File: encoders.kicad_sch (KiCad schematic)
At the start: 110 parts, among them U1 PEL12T-4225S-S1024, U10 WS2811F, U11 WS2811F, U12 WS2811F, U13 WS2811F, U14 WS2811F, U15 WS2811F, U16 WS2811F, U2 PEL12T-4225S-S1024, U3 PEL12T-4225S-S1024, U30 MCP23S17_SS, U31 MCP23S17_SS, U4 PEL12T-4225S-S1024, U5 PEL12T-4225S-S1024, U6 PEL12T-4225S-S1024, U7 PEL12T-4225S-S1024, U8 PEL12T-4225S-S1024, U9 WS2811F

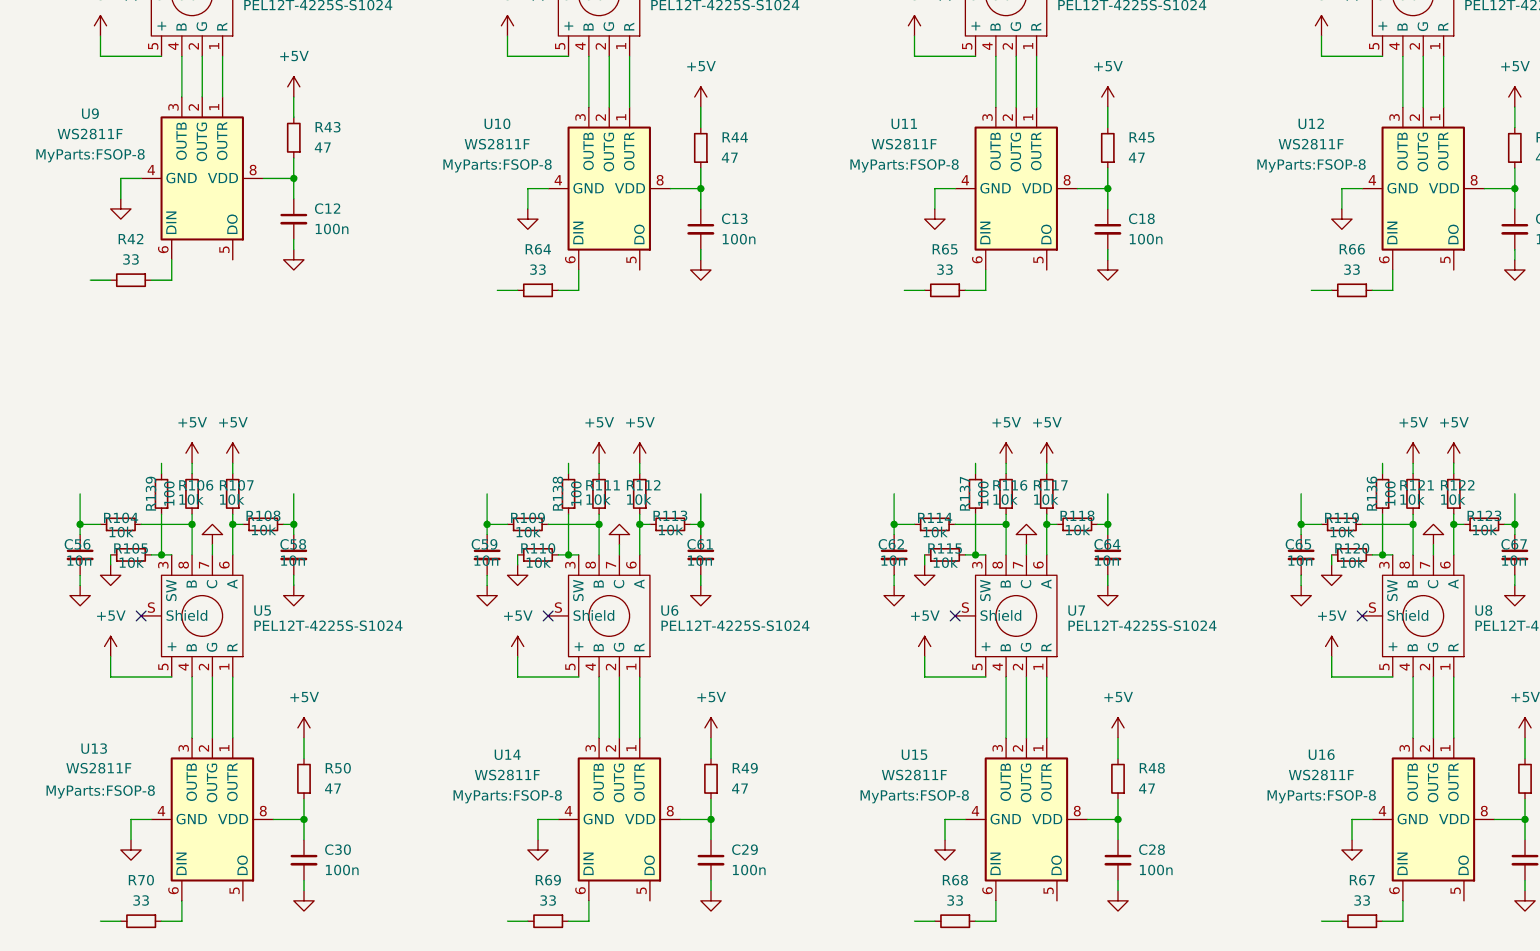
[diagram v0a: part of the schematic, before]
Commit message: rename symbol & footprint libs
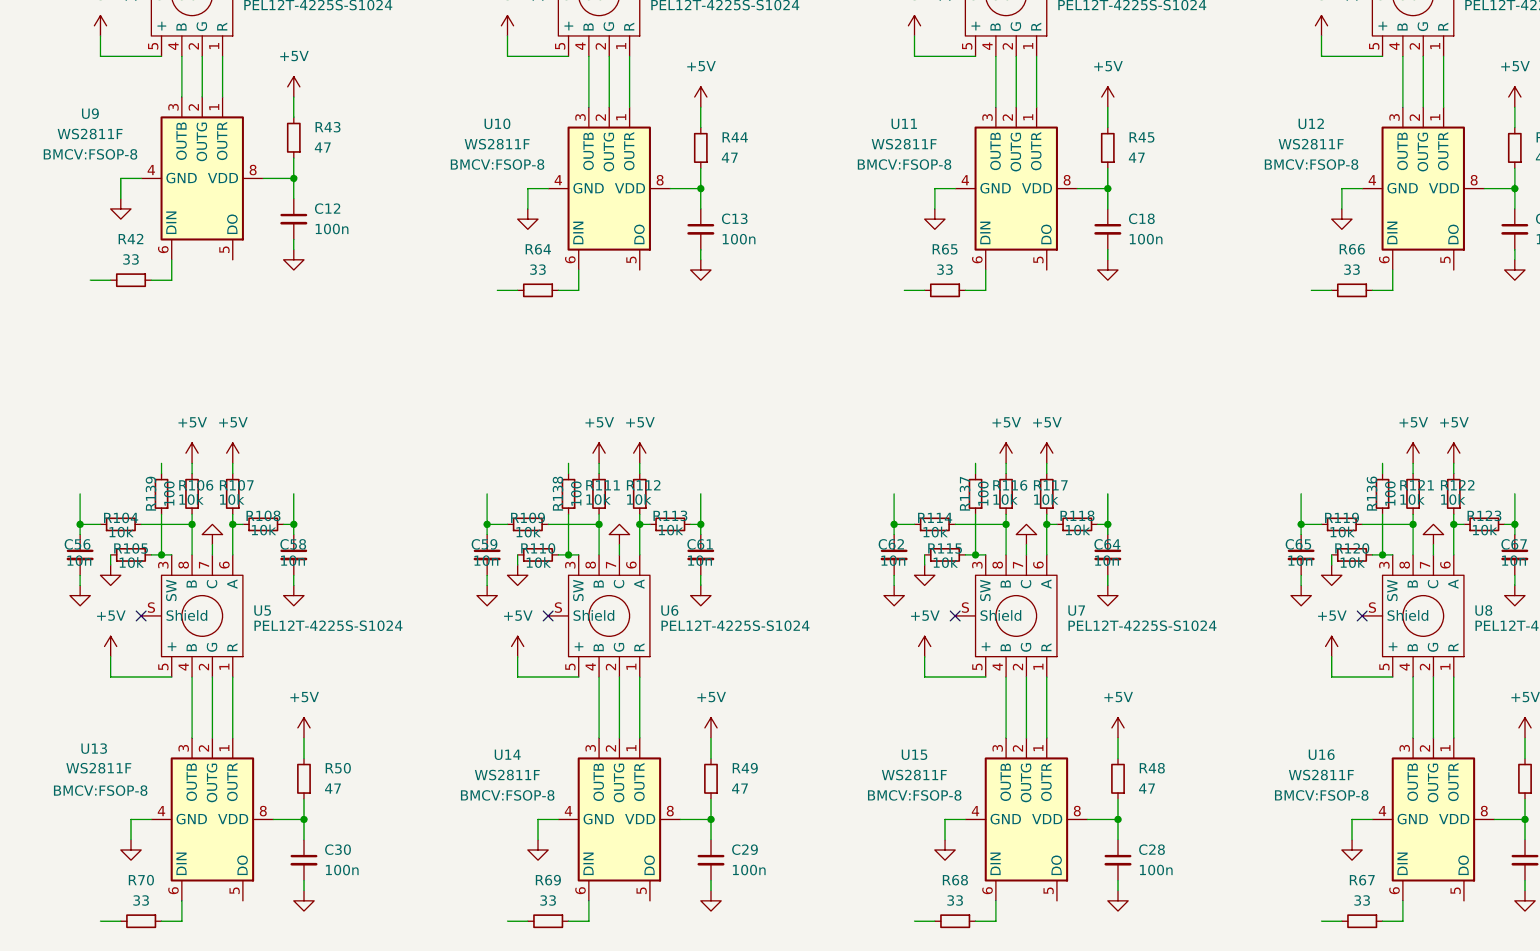
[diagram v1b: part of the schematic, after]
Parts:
- U1, U2, U3, U4, U5, U6, U7, U8: footprint MyParts:PEL12T-4xxxS-S1024 -> BMCV:PEL12T-4xxxS-S1024; symbol MySymbols:EC12PLRGBSDVBF -> BMCV:EC12PLRGBSDVBF
- U10, U11, U12, U13, U14, U15, U16, U9: footprint MyParts:FSOP-8 -> BMCV:FSOP-8; symbol MySymbols:WS2811 -> BMCV:WS2811
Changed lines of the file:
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@@
 	)
 	(symbol
-		(lib_id "MySymbols:EC12PLRGBSDVBF")
+		(lib_id "BMCV:EC12PLRGBSDVBF")
 		(at 39.37 115.57 180)
 		(unit 1)
@@
 			)
 		)
-		(property "Footprint" "MyParts:PEL12T-4xxxS-S1024"
+		(property "Footprint" "BMCV:PEL12T-4xxxS-S1024"
 			(at 39.37 115.57 0)
 			(effects
@@
 	)
 	(symbol
-		(lib_id "MySymbols:EC12PLRGBSDVBF")
+		(lib_id "BMCV:EC12PLRGBSDVBF")
 		(at 191.77 115.57 180)
 		(unit 1)
@@
 			)
 		)
-		(property "Footprint" "MyParts:PEL12T-4xxxS-S1024"
+		(property "Footprint" "BMCV:PEL12T-4xxxS-S1024"
 			(at 191.77 115.57 0)
 			(effects
@@
 	)
 	(symbol
-		(lib_id "MySymbols:EC12PLRGBSDVBF")
+		(lib_id "BMCV:EC12PLRGBSDVBF")
 		(at 190.5 38.1 180)
 		(unit 1)
@@
 			)
 		)
-		(property "Footprint" "MyParts:PEL12T-4xxxS-S1024"
+		(property "Footprint" "BMCV:PEL12T-4xxxS-S1024"
 			(at 190.5 38.1 0)
 			(effects
@@
 	)
 	(symbol
-		(lib_id "MySymbols:EC12PLRGBSDVBF")
+		(lib_id "BMCV:EC12PLRGBSDVBF")
 		(at 140.97 115.57 180)
 		(unit 1)
@@
 			)
 		)
-		(property "Footprint" "MyParts:PEL12T-4xxxS-S1024"
+		(property "Footprint" "BMCV:PEL12T-4xxxS-S1024"
 			(at 140.97 115.57 0)
 			(effects
@@
 	)
 	(symbol
-		(lib_id "MySymbols:WS2811")
+		(lib_id "BMCV:WS2811")
 		(at 140.97 62.23 270)
 		(mirror x)
@@
 			)
 		)
-		(property "Footprint" "MyParts:FSOP-8"
+		(property "Footprint" "BMCV:FSOP-8"
 			(at 127 59.2738 90)
 			(effects
@@
 	)
 	(symbol
-		(lib_id "MySymbols:EC12PLRGBSDVBF")
+		(lib_id "BMCV:EC12PLRGBSDVBF")
 		(at 90.17 115.57 180)
 		(unit 1)
@@
 			)
 		)
-		(property "Footprint" "MyParts:PEL12T-4xxxS-S1024"
+		(property "Footprint" "BMCV:PEL12T-4xxxS-S1024"
 			(at 90.17 115.57 0)
 			(effects
@@
 	)
 	(symbol
-		(lib_id "MySymbols:WS2811")
+		(lib_id "BMCV:WS2811")
 		(at 90.17 62.23 270)
 		(mirror x)
@@
 			)
 		)
-		(property "Footprint" "MyParts:FSOP-8"
+		(property "Footprint" "BMCV:FSOP-8"
 			(at 76.2 59.2738 90)
 			(effects
@@
 	)
 	(symbol
-		(lib_id "MySymbols:WS2811")
+		(lib_id "BMCV:WS2811")
 		(at 193.04 140.97 270)
 		(mirror x)
@@
 			)
 		)
-		(property "Footprint" "MyParts:FSOP-8"
+		(property "Footprint" "BMCV:FSOP-8"
 			(at 179.07 138.0138 90)
 			(effects
@@
 	)
 	(symbol
-		(lib_id "MySymbols:EC12PLRGBSDVBF")
+		(lib_id "BMCV:EC12PLRGBSDVBF")
 		(at 88.9 38.1 180)
 		(unit 1)
@@
 			)
 		)
-		(property "Footprint" "MyParts:PEL12T-4xxxS-S1024"
+		(property "Footprint" "BMCV:PEL12T-4xxxS-S1024"
 			(at 88.9 38.1 0)
 			(effects
@@
 	)
 	(symbol
-		(lib_id "MySymbols:WS2811")
+		(lib_id "BMCV:WS2811")
 		(at 142.24 140.97 270)
 		(mirror x)
@@
 			)
 		)
-		(property "Footprint" "MyParts:FSOP-8"
+		(property "Footprint" "BMCV:FSOP-8"
 			(at 128.27 138.0138 90)
 			(effects
@@
 	)
 	(symbol
-		(lib_id "MySymbols:WS2811")
+		(lib_id "BMCV:WS2811")
 		(at 91.44 140.97 270)
 		(mirror x)
@@
 			)
 		)
-		(property "Footprint" "MyParts:FSOP-8"
+		(property "Footprint" "BMCV:FSOP-8"
 			(at 77.47 138.0138 90)
 			(effects
@@
 	)
 	(symbol
-		(lib_id "MySymbols:WS2811")
+		(lib_id "BMCV:WS2811")
 		(at 39.37 60.96 270)
 		(mirror x)
@@
 			)
 		)
-		(property "Footprint" "MyParts:FSOP-8"
+		(property "Footprint" "BMCV:FSOP-8"
 			(at 25.4 58.0038 90)
 			(effects
@@
 	)
 	(symbol
-		(lib_id "MySymbols:EC12PLRGBSDVBF")
+		(lib_id "BMCV:EC12PLRGBSDVBF")
 		(at 139.7 38.1 180)
 		(unit 1)
@@
 			)
 		)
-		(property "Footprint" "MyParts:PEL12T-4xxxS-S1024"
+		(property "Footprint" "BMCV:PEL12T-4xxxS-S1024"
 			(at 139.7 38.1 0)
 			(effects
@@
 	)
 	(symbol
-		(lib_id "MySymbols:WS2811")
+		(lib_id "BMCV:WS2811")
 		(at 191.77 62.23 270)
 		(mirror x)
@@
 			)
 		)
-		(property "Footprint" "MyParts:FSOP-8"
+		(property "Footprint" "BMCV:FSOP-8"
 			(at 177.8 59.2738 90)
 			(effects
@@
 	)
 	(symbol
-		(lib_id "MySymbols:WS2811")
+		(lib_id "BMCV:WS2811")
 		(at 40.64 140.97 270)
 		(mirror x)
@@
 			)
 		)
-		(property "Footprint" "MyParts:FSOP-8"
+		(property "Footprint" "BMCV:FSOP-8"
 			(at 26.67 137.414 90)
 			(effects
@@
 	)
 	(symbol
-		(lib_id "MySymbols:EC12PLRGBSDVBF")
+		(lib_id "BMCV:EC12PLRGBSDVBF")
 		(at 38.1 38.1 180)
 		(unit 1)
@@
 			)
 		)
-		(property "Footprint" "MyParts:PEL12T-4xxxS-S1024"
+		(property "Footprint" "BMCV:PEL12T-4xxxS-S1024"
 			(at 38.1 38.1 0)
 			(effects

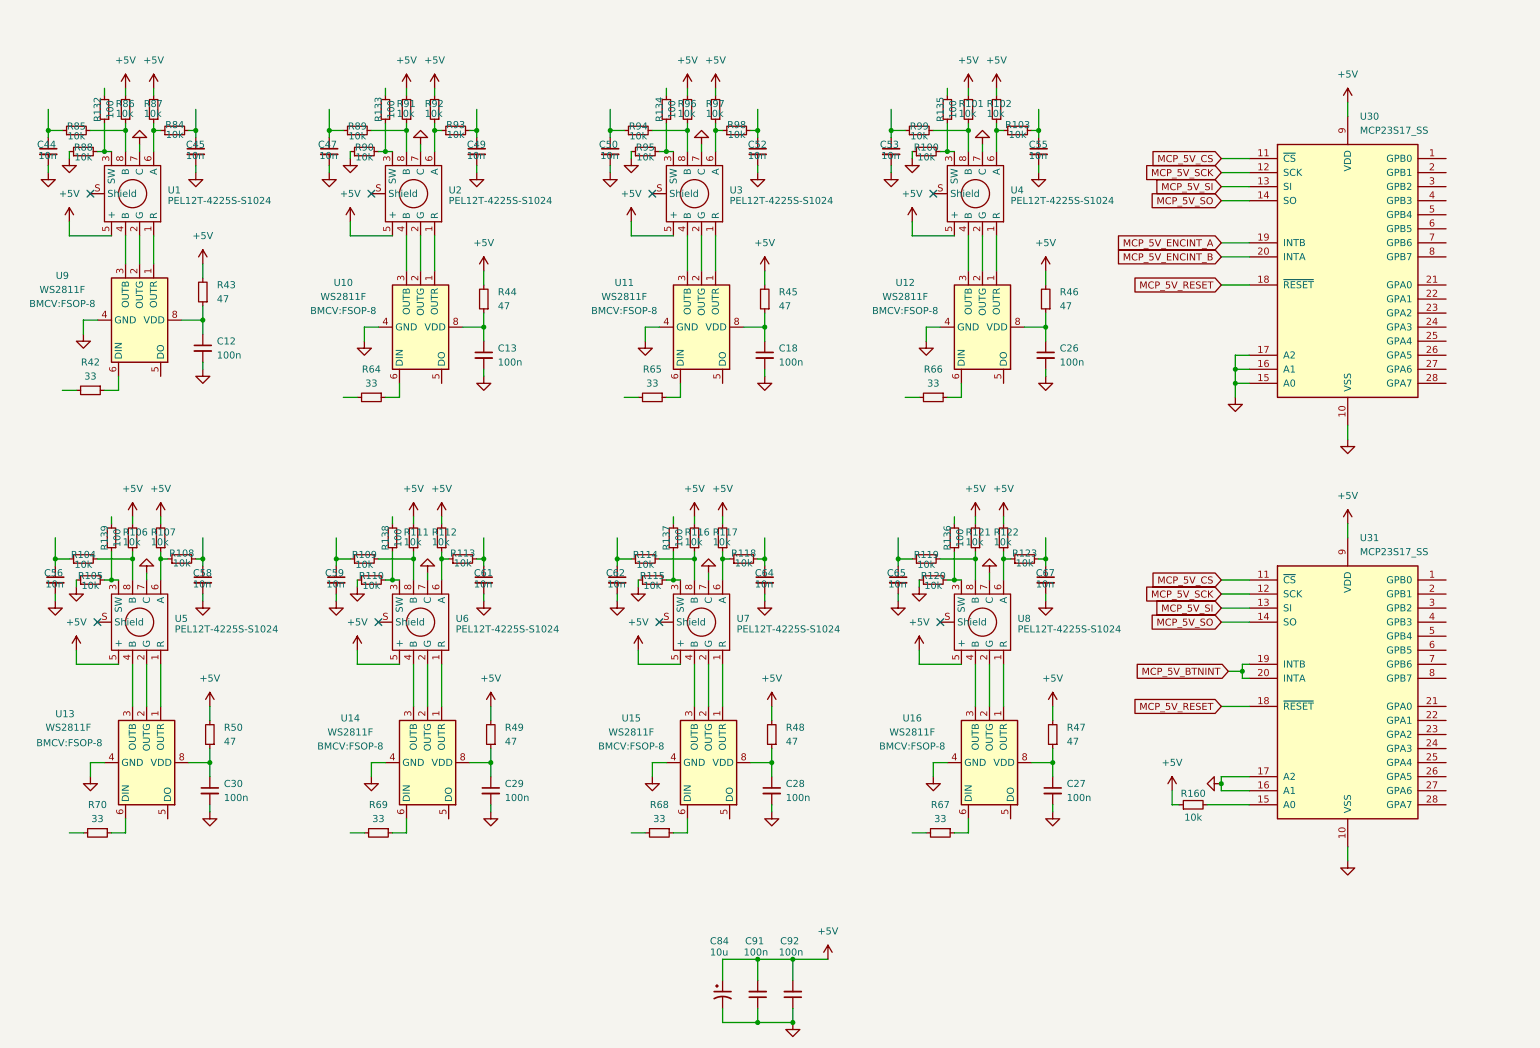
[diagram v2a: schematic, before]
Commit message: routing progress (bottom buttons & encoders)
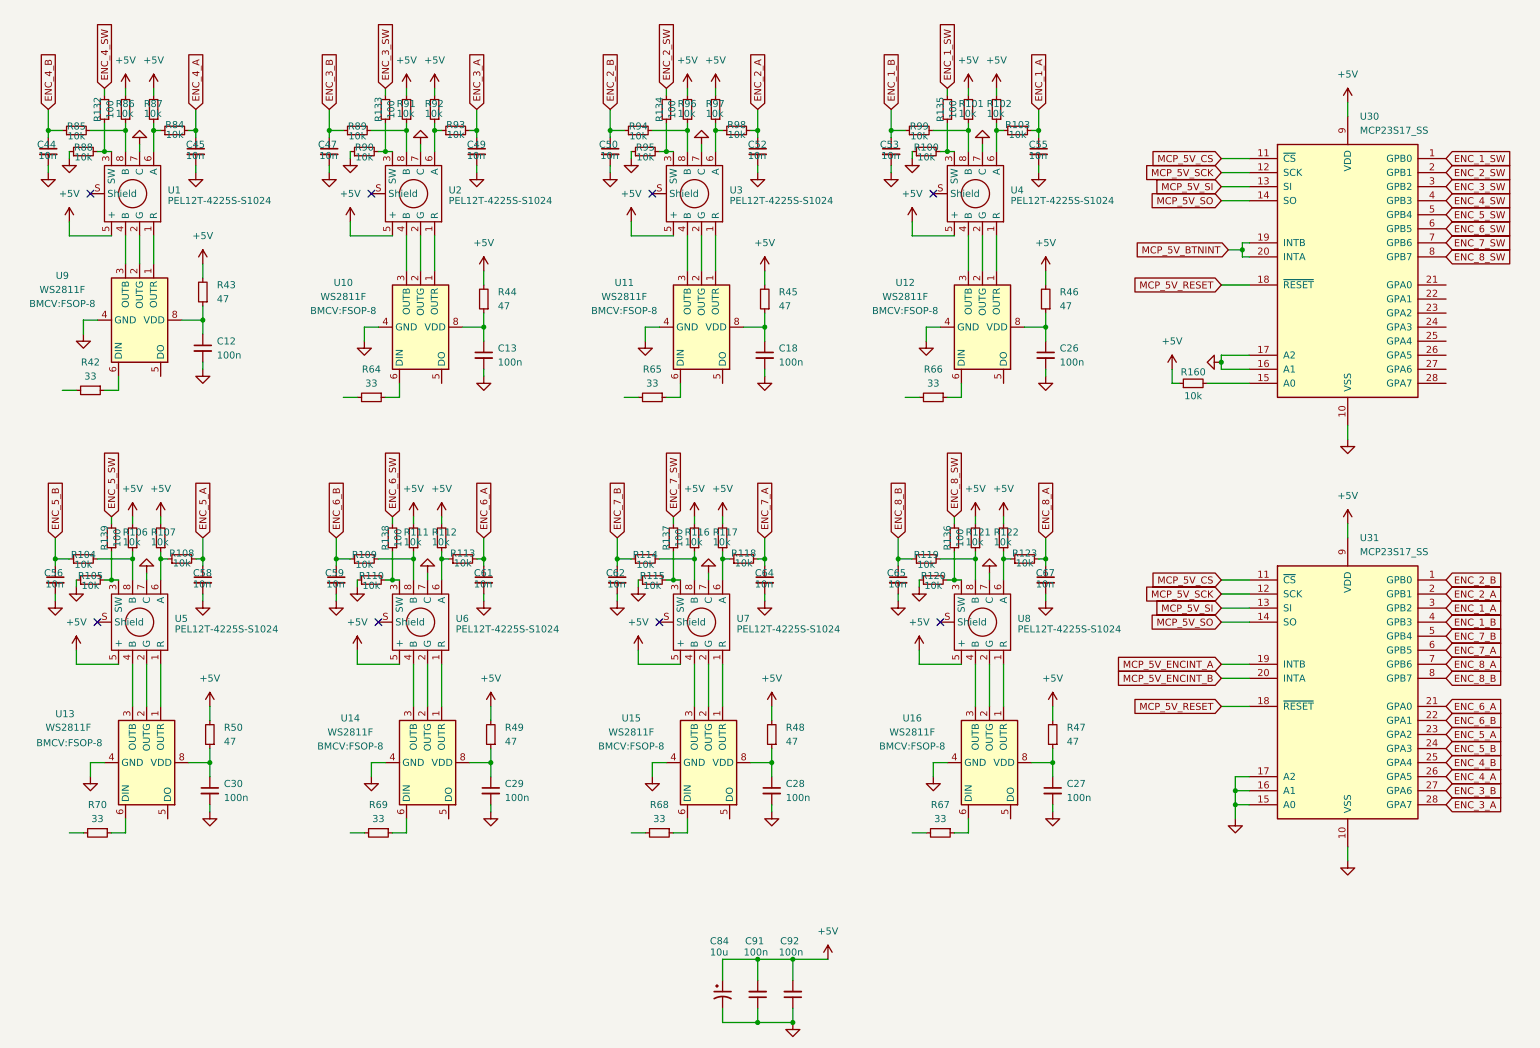
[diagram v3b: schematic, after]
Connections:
- net GND: now also U31.15 (A0); no longer U30.15 (A0)
- net MCP_5V_BTNINT: now also U30.19 (INTB), U30.20 (INTA); no longer U31.19 (INTB), U31.20 (INTA)
- net MCP_5V_ENCINT_A: now also U31.19 (INTB); no longer U30.19 (INTB)
- net MCP_5V_ENCINT_B: now also U31.20 (INTA); no longer U30.20 (INTA)
- net ENC_3_B: now reaches C47.1, R89.1
- net ENC_3_B: now also U31.27 (GPA6)
- net ENC_5_A: now reaches C58.1, R108.2
- net ENC_5_A: now also U31.23 (GPA2)
- net ENC_7_A: now reaches C64.1, R118.2
- net ENC_7_A: now also U31.6 (GPB5)
- net ENC_1_A: now reaches C55.1, R103.2
- net ENC_1_A: now also U31.3 (GPB2)
- net ENC_5_B: now reaches C56.1, R104.1
- net ENC_5_B: now also U31.24 (GPA3)
- net ENC_8_B: now reaches C65.1, R119.1
- net ENC_8_B: now also U31.8 (GPB7)
- net ENC_2_A: now reaches C52.1, R98.2
- net ENC_2_A: now also U31.2 (GPB1)
- net ENC_4_A: now reaches C45.1, R84.2
- net ENC_4_A: now also U31.26 (GPA5)
- net ENC_8_A: now reaches C67.1, R123.2
- net ENC_8_A: now also U31.7 (GPB6)
- net ENC_4_B: now reaches C44.1, R85.1
- net ENC_4_B: now also U31.25 (GPA4)
- net ENC_2_B: now reaches C50.1, R94.1
- net ENC_2_B: now also U31.1 (GPB0)
- net ENC_1_SW: now reaches U30.1 (GPB0)
- net ENC_1_SW: now also R135.2
- net ENC_2_SW: now reaches U30.2 (GPB1)
- net ENC_2_SW: now also R134.2
- net ENC_3_SW: now reaches U30.3 (GPB2)
- net ENC_3_SW: now also R133.2
- net ENC_4_SW: now reaches U30.4 (GPB3)
- net ENC_4_SW: now also R132.2
- net ENC_5_SW: now reaches U30.5 (GPB4)
- net ENC_5_SW: now also R139.2
- net ENC_6_SW: now reaches U30.6 (GPB5)
- net ENC_6_SW: now also R138.2
- net ENC_7_SW: now reaches U30.7 (GPB6)
- net ENC_7_SW: now also R137.2
- net ENC_8_SW: now reaches U30.8 (GPB7)
- net ENC_8_SW: now also R136.2
- net ENC_3_A: now reaches C49.1, R93.2
- net ENC_3_A: now also U31.28 (GPA7)
- net ENC_1_B: now reaches C53.1, R99.1
- net ENC_1_B: now also U31.4 (GPB3)
- net ENC_6_A: now reaches C61.1, R113.2
- net ENC_6_A: now also U31.21 (GPA0)
- net ENC_6_B: now reaches C59.1, R109.1
- net ENC_6_B: now also U31.22 (GPA1)
- net ENC_7_B: now reaches C62.1, R114.1
- net ENC_7_B: now also U31.5 (GPB4)
- net at R160.2: now also U30.15 (A0); no longer U31.15 (A0)
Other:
- moved on the sheet: R160
